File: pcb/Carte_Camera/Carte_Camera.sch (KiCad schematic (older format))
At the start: 5 parts, among them J1 Samtec FTS-105-01-L-DV, U1 TSL1401CL

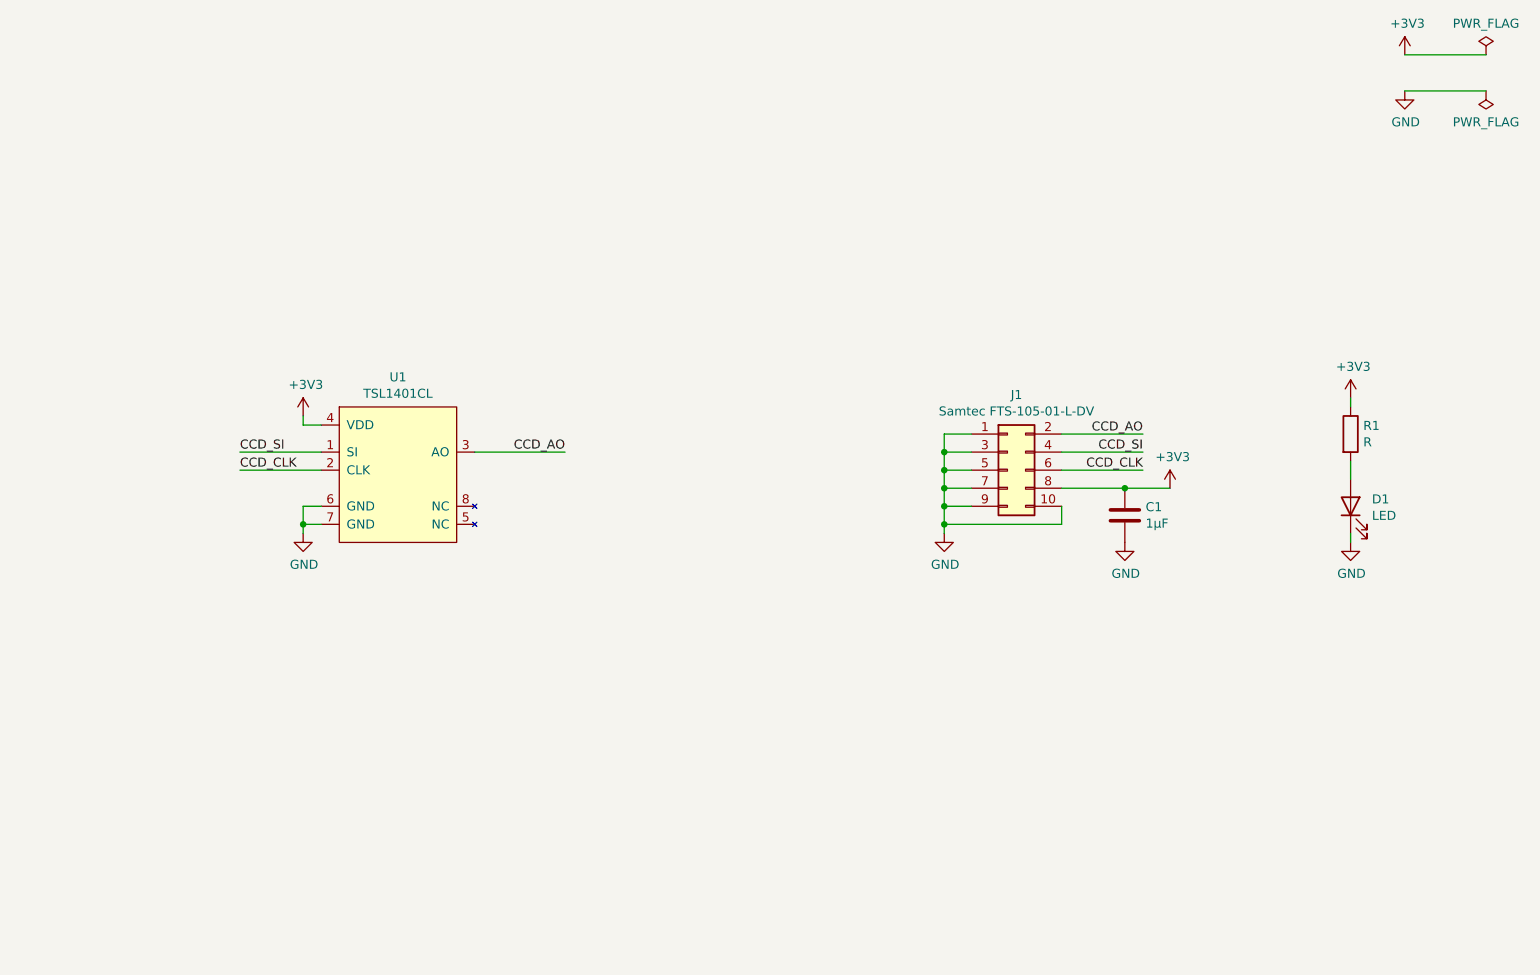
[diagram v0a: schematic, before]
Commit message: ajout de la carte chassi DFRobotics + creation d'une nouvelle carte led + creation d'une carte capteur pour DFRobotic + correction de l'alimentation en 5V des encodeurs sur DFRobotic (carte Landzo a corriger dans un prochaine commit)
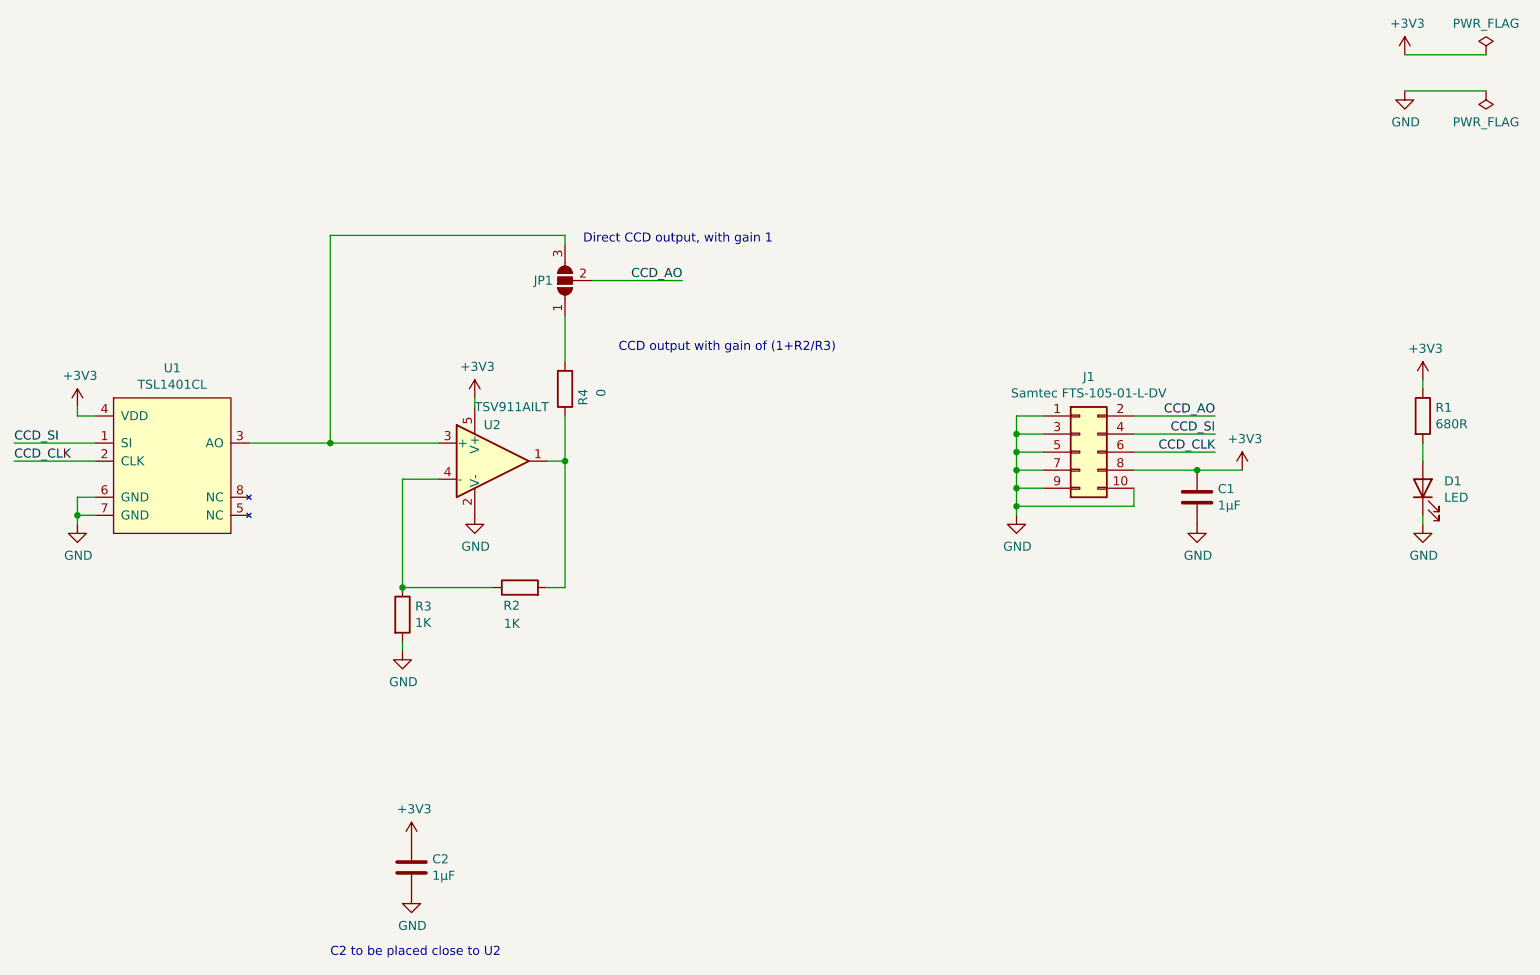
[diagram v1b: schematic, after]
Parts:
- added C2: 1µF, Capacitor_SMD:C_0805_2012Metric_Pad1.15x1.40mm_HandSolder, symbol Device:C
- added JP1: SolderJumper_3_Open, Jumper:SolderJumper-3_P1.3mm_Open_RoundedPad1.0x1.5mm_NumberLabels, symbol Jumper:SolderJumper_3_Open
- added R2, R3: 1K, Resistor_SMD:R_0805_2012Metric_Pad1.15x1.40mm_HandSolder, symbol Device:R
- added R4: 0, Resistor_SMD:R_0805_2012Metric_Pad1.15x1.40mm_HandSolder, symbol Device:R
- added U2: TSV911AILT, Package_TO_SOT_SMD:SOT-23-5, symbol Amplifier_Operational:TLV2371DBV
- C1: footprint Capacitor_SMD:C_1206_3216Metric_Pad1.42x1.75mm_HandSolder -> Capacitor_SMD:C_0805_2012Metric_Pad1.15x1.40mm_HandSolder
- D1: footprint LED_SMD:LED_1206_3216Metric_Pad1.42x1.75mm_HandSolder -> LED_SMD:LED_0805_2012Metric_Pad1.15x1.40mm_HandSolder
- R1: value R -> 680R; footprint Resistor_SMD:R_1206_3216Metric_Pad1.42x1.75mm_HandSolder -> Resistor_SMD:R_0805_2012Metric_Pad1.15x1.40mm_HandSolder
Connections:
- net +3V3: now also C2.1, U2.5 (V+)
- net CCD_AO: now also JP1.2 (C); no longer U1.3 (AO)
- net GND: now also C2.2, R3.2, U2.2 (V-)
- new net: JP1.3 (B), U1.3 (AO), U2.3 (+)
- new net: R2.2, R4.1, U2.1
- new net: R2.1, R3.1, U2.4 (-)
- new net: JP1.1 (A), R4.2
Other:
- note added: "C2 to be placed close to U2"
- note added: "CCD output with gain of (1+R2/R3)"
- note added: "Direct CCD output, with gain 1"
- moved on the sheet: C1, D1, J1, R1, U1
